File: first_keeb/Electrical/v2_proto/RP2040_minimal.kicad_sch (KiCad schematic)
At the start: 65 parts, among them P1 USB_C_Receptacle, Q1 BSS138, SW1 SW_Push, SW2 SW_Push, U1 NCP1117-3.3_SOT223, U2 LM4040DBZ-3, U3 W25Q128JVS, U4 RP2040, U5 PRTR5V0U2X, Y1 ABM7-12.000MHZ-D2Y-T

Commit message: finishes proto_2 pcb
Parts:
- removed H2, H3, H4: MountingHole, MountingHole:MountingHole_2.2mm_M2, symbol Mechanical:MountingHole
- added C27: 1u, Capacitor_SMD:C_0402_1005Metric, symbol Device:C
- added D6: WS2812B, LED_SMD:LED_WS2812B_PLCC4_5.0x5.0mm_P3.2mm, symbol LED:WS2812B
- H: renamed from H1; footprint MountingHole:MountingHole_2.2mm_M2 -> MountingHole:MountingHole_2.7mm_M2.5
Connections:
- net GPIO10 is gone; now on net BUTT0: U4.13 (GPIO10)
- net GPIO11 is gone; now on net BUTT1: U4.14 (GPIO11)
- net GPIO12 is gone; now on net LED_D_3V3: U4.15 (GPIO12)
- net GND: now also C27.2, D6.3 (VSS)
- net VBUS: now also C27.1, D6.1 (VDD)
- net at D1.3 (DIN): now also D6.2 (DOUT); no longer D5.2 (DOUT)
- new net: D5.2 (DOUT), D6.4 (DIN)

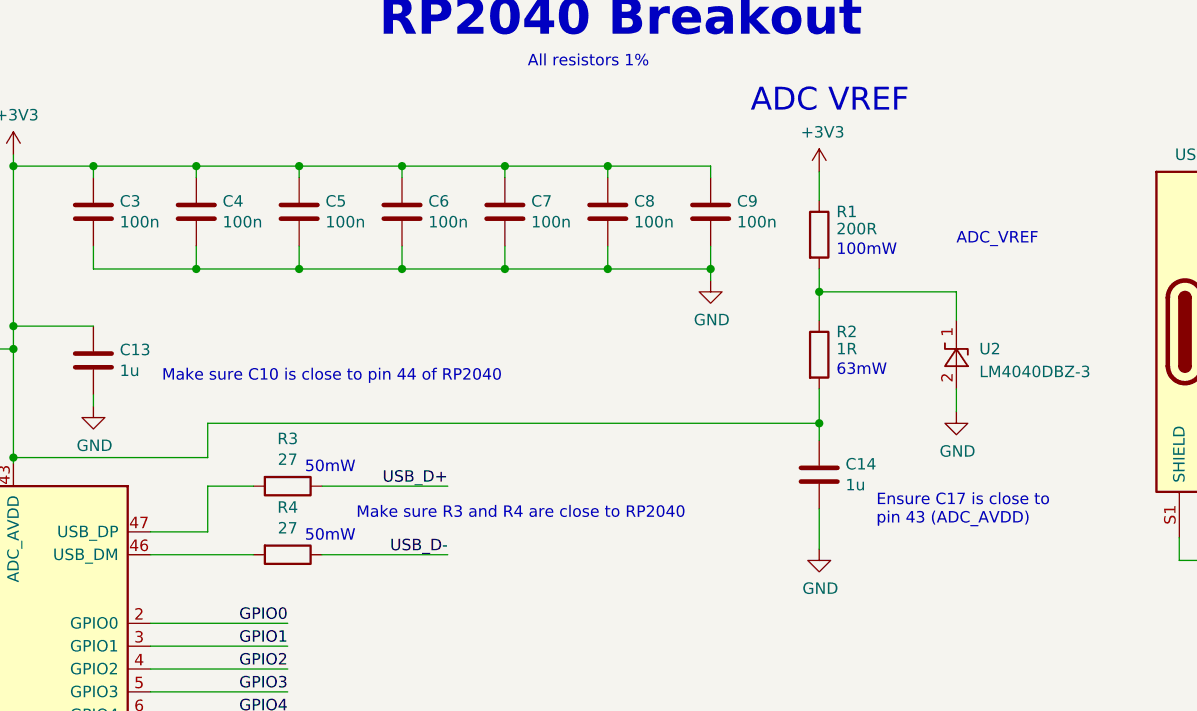
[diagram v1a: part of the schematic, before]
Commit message: ads voltage reference
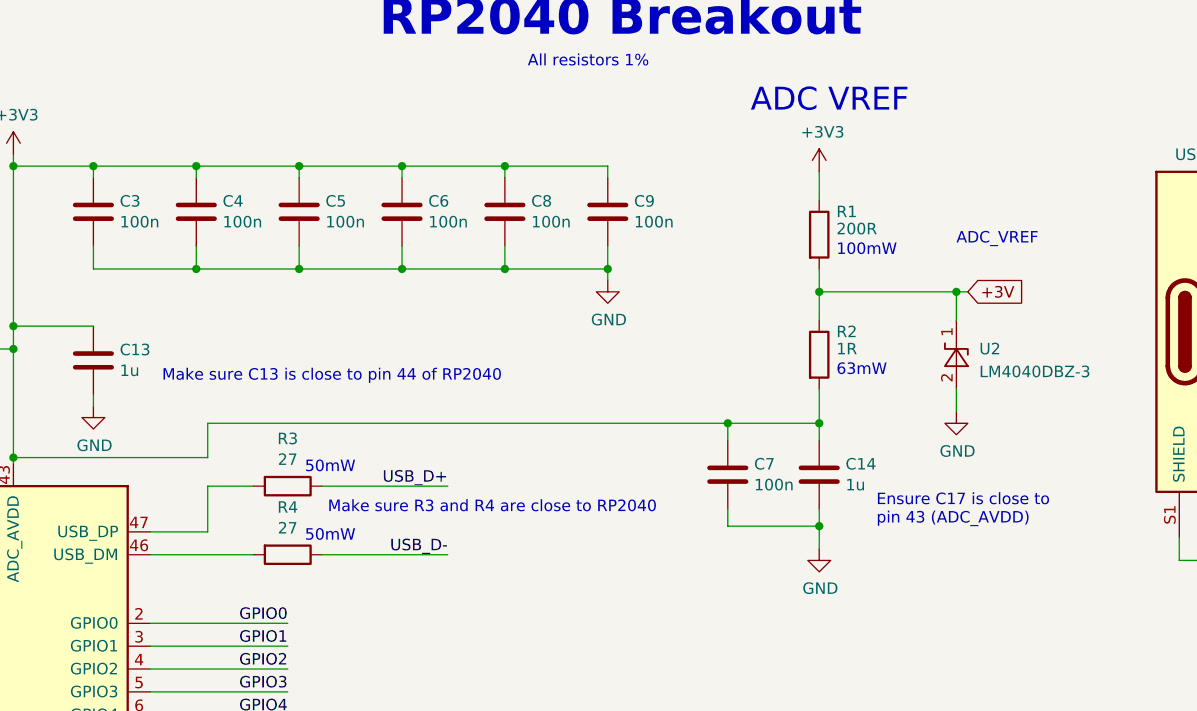
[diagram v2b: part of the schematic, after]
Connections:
- net +3V: now reaches R1.2, R2.1, U2.1 (K)
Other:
- note added: "Make sure C13 is close to pin 44 of RP2040"
- note removed: "Make sure C10 is close to pin 44 of RP2040"
- moved on the sheet: C8, C9

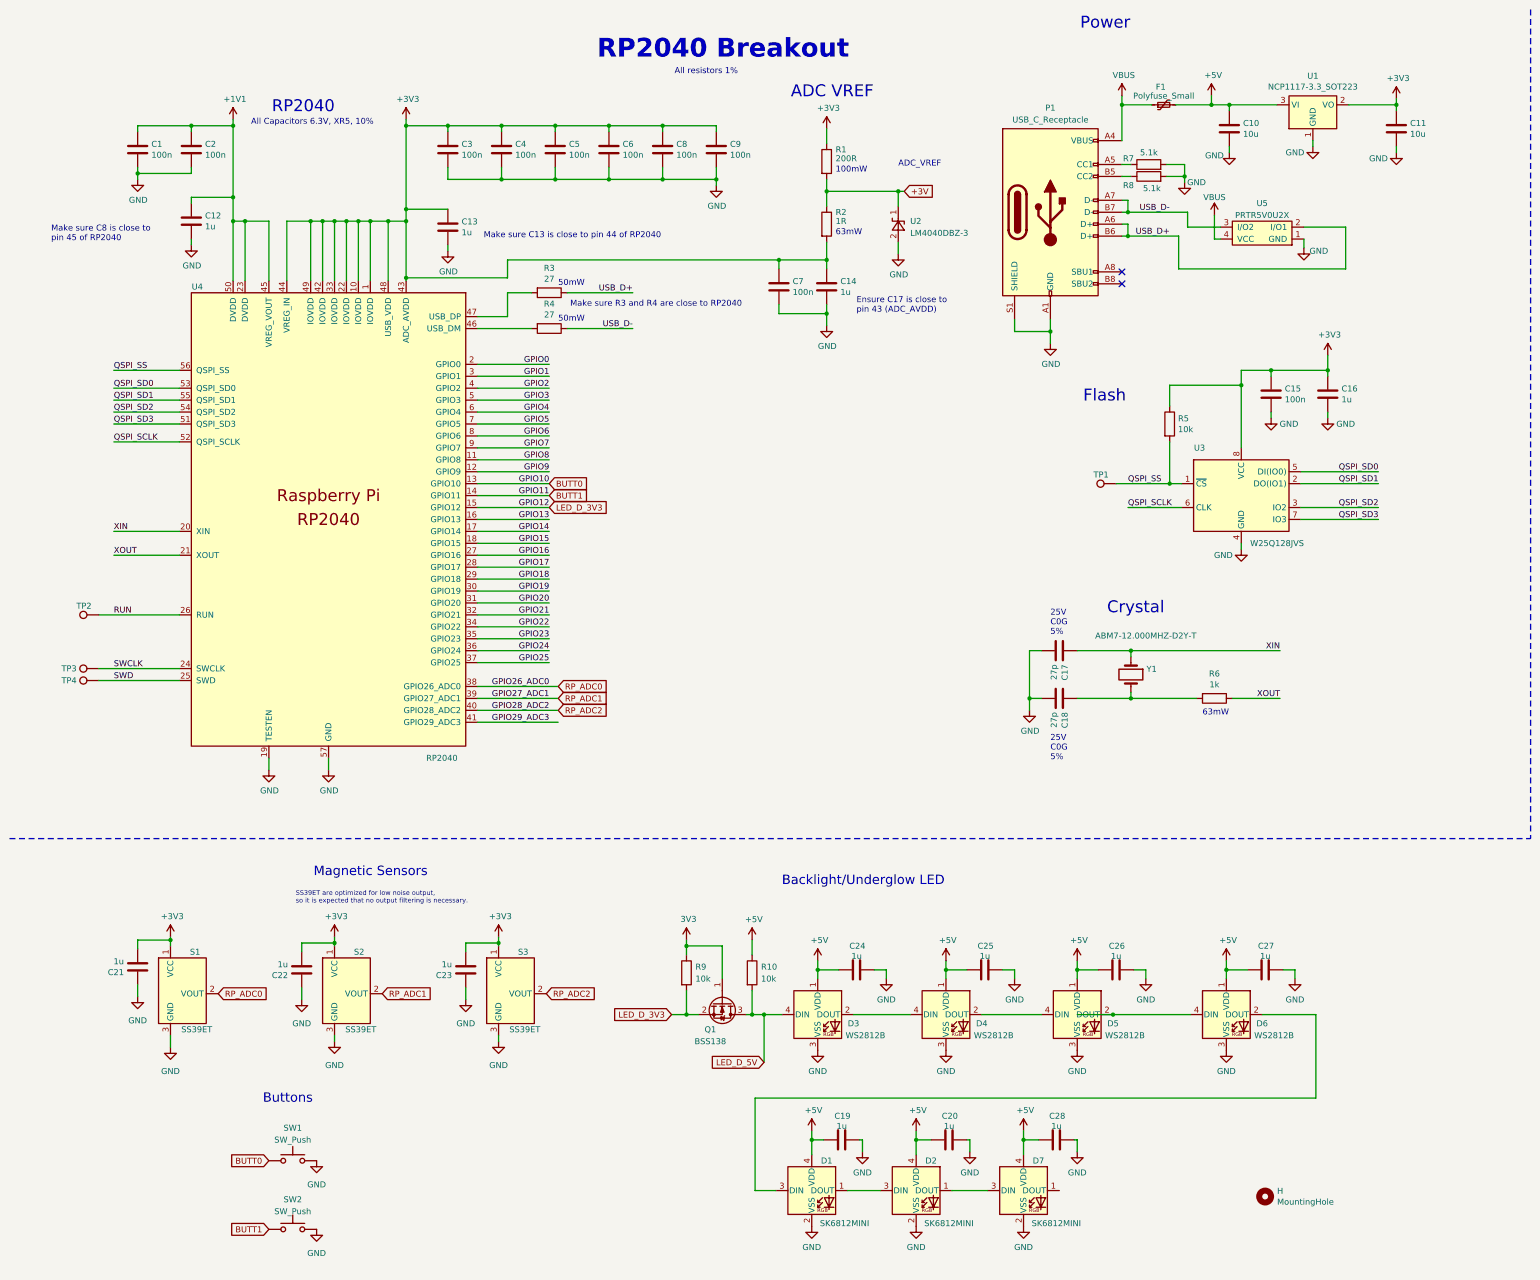
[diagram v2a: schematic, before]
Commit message: finishes proto_v2 board. Set up some stuff to automate jlcpcb format for pcb assembly
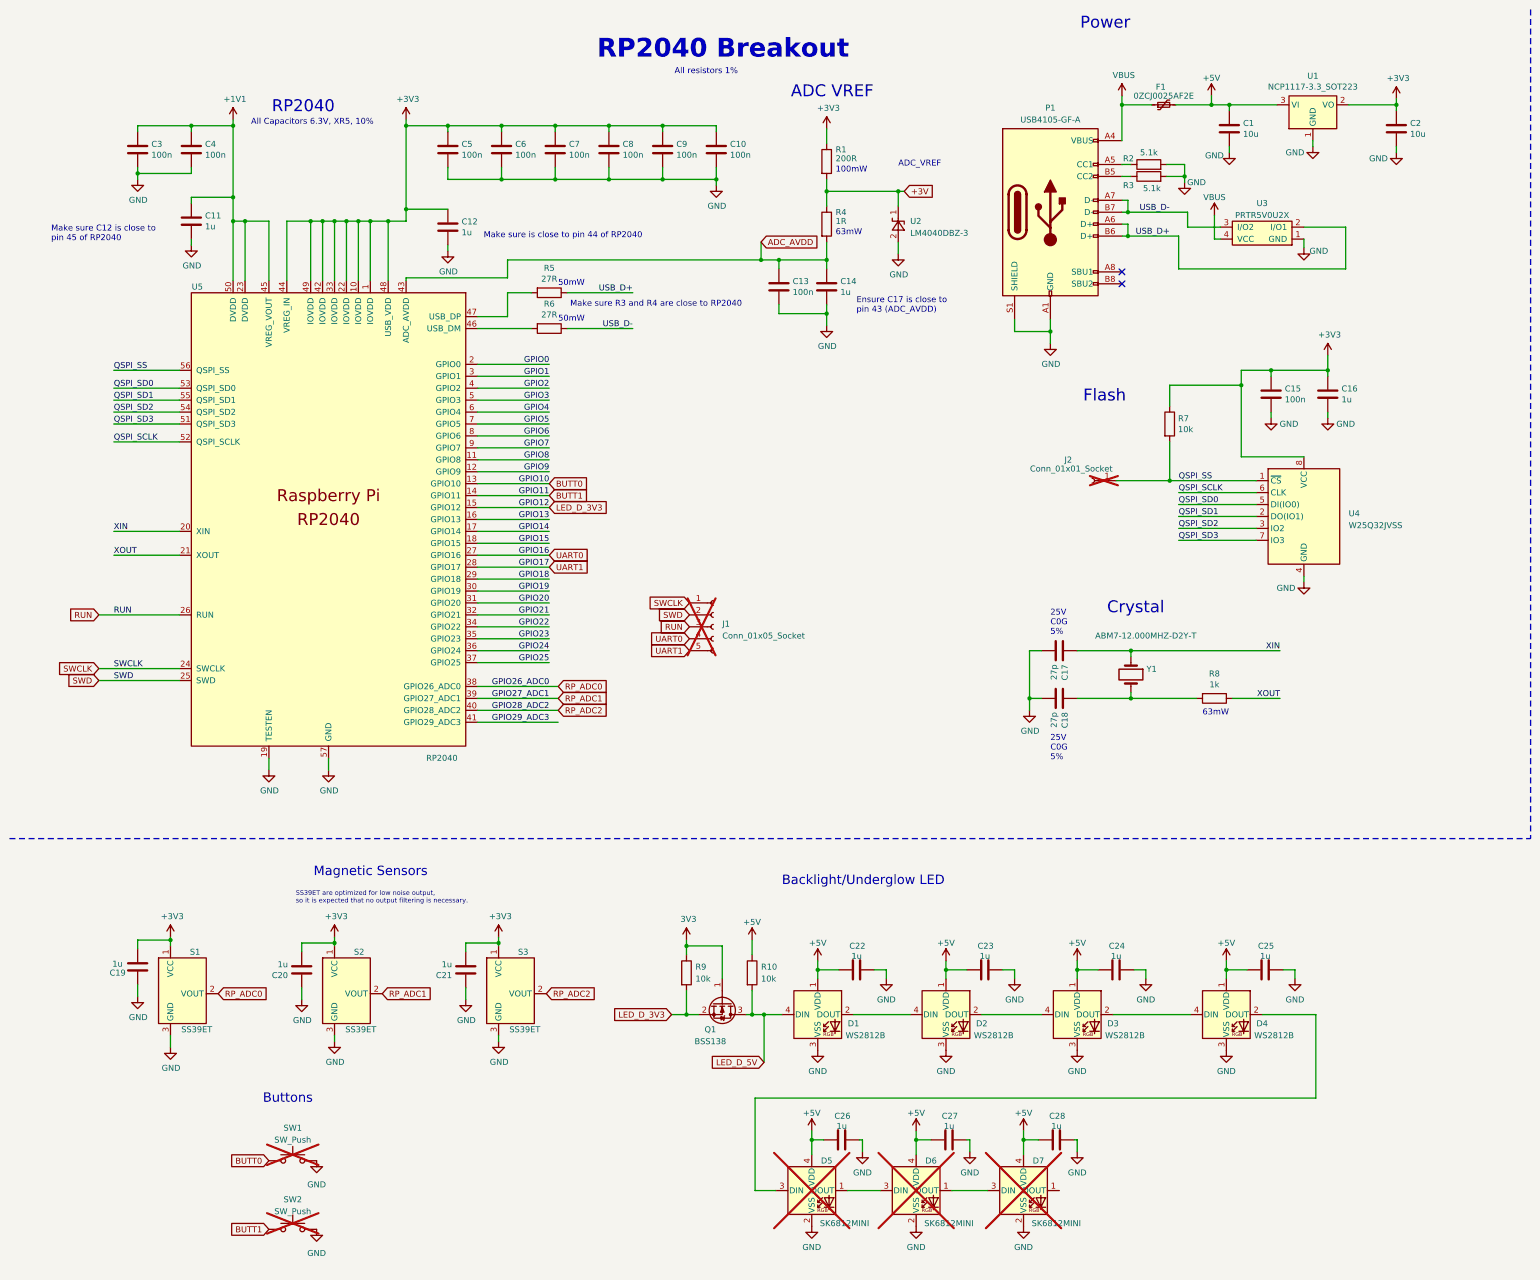
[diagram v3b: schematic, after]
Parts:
- removed H: MountingHole, MountingHole:MountingHole_2.7mm_M2.5, symbol Mechanical:MountingHole
- removed TP1, TP2, TP3, TP4: TestPoint, symbol Connector:TestPoint
- removed U3: W25Q128JVS, Package_SO:SOIC-8_5.23x5.23mm_P1.27mm, symbol RP2040_minimal-rescue:W25Q128JVS-Memory_Flash
- added J1: Conn_01x05_Socket, Connector_PinSocket_2.54mm:PinSocket_1x05_P2.54mm_Vertical, symbol Connector:Conn_01x05_Socket
- added J2: Conn_01x01_Socket, Connector_PinSocket_2.54mm:PinSocket_1x01_P2.54mm_Vertical, symbol Connector:Conn_01x01_Socket
- added U4: W25Q32JVSS, Package_SO:SOIC-8_5.23x5.23mm_P1.27mm, symbol Memory_Flash:W25Q32JVSS
- D5: renamed from D1; now not fitted
- D6: renamed from D2; now not fitted
- D7, SW1, SW2: now not fitted
- F1: value Polyfuse_Small -> 0ZCJ0025AF2E
- P1: value USB_C_Receptacle -> USB4105-GF-A
- R4: renamed from R2; footprint Capacitor_SMD:C_0402_1005Metric -> Capacitor_SMD:C_0603_1608Metric
- R5: renamed from R3; value 27 -> 27R
- R6: renamed from R4; value 27 -> 27R
- renumbered C10 to C1, C9 to C10, C12 to C11, C13 to C12, C7 to C13, C21 to C19, C11 to C2, C22 to C20, C23 to C21, C24 to C22, C25 to C23, C26 to C24, C27 to C25, C19 to C26, C20 to C27, C1 to C3, C2 to C4, C3 to C5, C4 to C6, C5 to C7, C6 to C8, C8 to C9, D3 to D1, D4 to D2, D5 to D3, D6 to D4, R7 to R2, R8 to R3, R5 to R7, R6 to R8, U5 to U3, U4 to U5
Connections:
- net GNDA is gone; now on net GND: C19.1, C20.1, C21.1, S1.3 (GND), S2.3 (GND), S3.3 (GND)
- net +3V3: now also U4.8 (VCC); no longer C13.1, C14.1, R4.2, U5.43 (ADC_AVDD)
- net GND: now also U4.4 (GND)
- net QSPI_SCLK: now also U4.6 (CLK)
- net QSPI_SD0: now also U4.5 (DI(IO0))
- net QSPI_SD1: now also U4.2 (DO(IO1))
- net QSPI_SD2: now also U4.3 (IO2)
- net QSPI_SD3: now also U4.7 (IO3)
- net QSPI_SS: now also J2.1 (Pin_1), U4.1 (~{CS})
- net RUN: now also J1.3 (Pin_3)
- net SWCLK: now also J1.1 (Pin_1)
- net SWD: now also J1.2 (Pin_2)
- net VBUS: no longer C1.1, C22.1, C23.1, C24.1, C25.1, C26.1, C27.1, C28.1, D1.1 (VDD), D2.1 (VDD), D3.1 (VDD), D4.1 (VDD), D5.4 (VDD), D6.4 (VDD), D7.4 (VDD), F1.2, R10.1, U1.3 (VI)
- net GPIO16 renamed UART0
- net UART0: now also J1.4 (Pin_4)
- net GPIO17 renamed UART1
- net UART1: now also J1.5 (Pin_5)
- new net +5V: C1.1, C22.1, C23.1, C24.1, C25.1, C26.1, C27.1, C28.1, D1.1 (VDD), D2.1 (VDD), D3.1 (VDD), D4.1 (VDD), D5.4 (VDD), D6.4 (VDD), D7.4 (VDD), F1.2, R10.1, U1.3 (VI)
- new net ADC_AVDD: C13.1, C14.1, R4.2, U5.43 (ADC_AVDD)
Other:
- note added: "Make sure C12 is close to pin 45 of RP2040"
- note added: "Make sure is close to pin 44 of RP2040"
- note removed: "Make sure C13 is close to pin 44 of RP2040"
- note removed: "Make sure C8 is close to pin 45 of RP2040"
